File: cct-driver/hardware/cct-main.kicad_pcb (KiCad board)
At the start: 2 copper layers, 110 x 145 mm, 205 parts, among them J1 C707824, J10 C37815, J11 C474923, J2 C165948, J3 C441333, J4 C441333, J5 C441333, J6 C441333, J7 C441333, J8 C441333, J9 C2906270, Q1 C3281500, Q10 C2890395, Q11 C2890395, Q12 C2890395, Q13 C2890395, Q14 C2890395, Q15 C2890395, Q16 C2890395, Q17 C2890395, Q18 C2890395, Q2 C3281500, Q3 C20526, Q4 C2146, Q5 C2146, Q6 C20526, Q7 C2890395, Q8 C2890395, Q9 C2890395, SW1 C318884, SW2 C318884, U1 C2864837, U2 C524806, U3 C6186, U4 C701341, U5 C84681, U6 C52140501, U7 C52140501

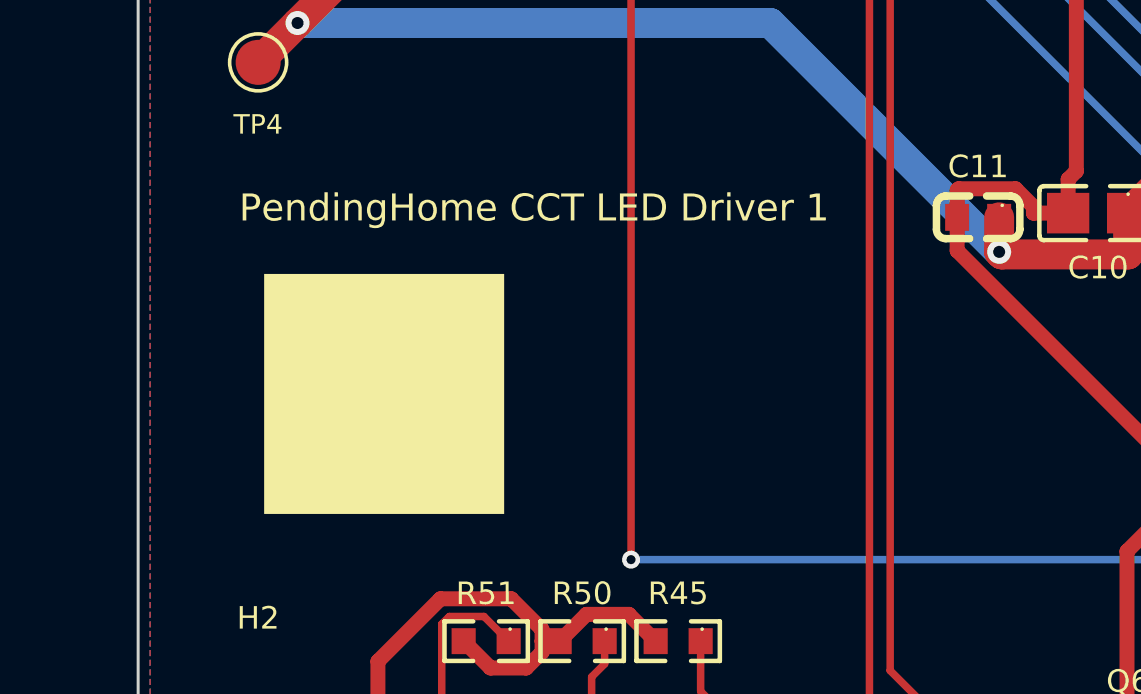
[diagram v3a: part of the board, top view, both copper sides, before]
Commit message: 板名改成白油块右侧两行
按人类要求把 `PendingHome CCT LED Driver 1` 拆成两行放到订单二维码白油块的
右侧:上行 `PendingHome`、下行 `CCT LED Driver 1`,左端对齐,与白块垂直居中。
原来那一行是单行横排压在白块上方,横跨 x2.26–24.14。

实现在 gen_silk.py 里(不手改 kicad_pcb):
- label() 加 left=True,用 KiCad 自己的左对齐,不靠脚本那套估算宽度去凑,
  两行左端因此严格对齐在 x=13.2
- 板名单独抽成 board_name(),常数写在一处:NAME_X=13.2(离白块右沿 1.0mm)、
  NAME_CY=53.2(= 白块中心)、size 0.9 bold、行距 1.5mm(字高 0.9,行间净空 0.6)
- 新增 `--boardname-only` 模式,**幂等**:先删掉板上已有的板名文字再放新的,
  重跑结果一模一样,不会像整份 gen_silk 那样重复堆文字
- 顺带补上一处漏洞:原来的障碍收集只看封装自带丝印,**板级丝印图形(那块白油)
  根本没进障碍表**。现在加进去了,所以「离白块 1.0mm」是真量出来的
- 放之前逐行实测净空并 assert,两行报出来的最近障碍都是白油块、都是 1.00mm

验收数字:
- 除 F_Silkscreen 外**全部 10 层逐字节相同**(F_Cu / B_Cu / F_Mask / B_Mask /
  F_Paste / B_Paste / B_Silkscreen / Edge_Cuts / PTH.drl / NPTH.drl,剔头部时间戳)
- F_Silkscreen 坐标点数 19382 → 19382 不变;差异点 424 出 424 进,
  出的包围盒 (2.66,46.51)–(23.79,47.71) = 旧那一行,
  进的包围盒 (13.49,51.96)–(24.89,54.36) = 新那两行,**全板其余丝印一个点没动**
- cpl-jlc.csv / pos-raw.csv / bom-jlc.csv / bom.csv **零变化**
- DRC 88 → 88 条,七类逐项相同,丝印三类 53/10/9 一条没多;netclass 检查通过
- 渲染出图看过:两行在白块右侧、左端齐、正读、上下不压 C10/R5/C11 与 R51/R50/R45

order-checklist 的认包特征跟着更新:F_Silkscreen 495,581 → **495,768 字节**,
「怎么认这个包」和下单前必查里的板名描述改成两行+右侧+实测坐标范围。
render-top/bottom.png 重新生成。

Co-Authored-By: Claude <noreply@anthropic.com>
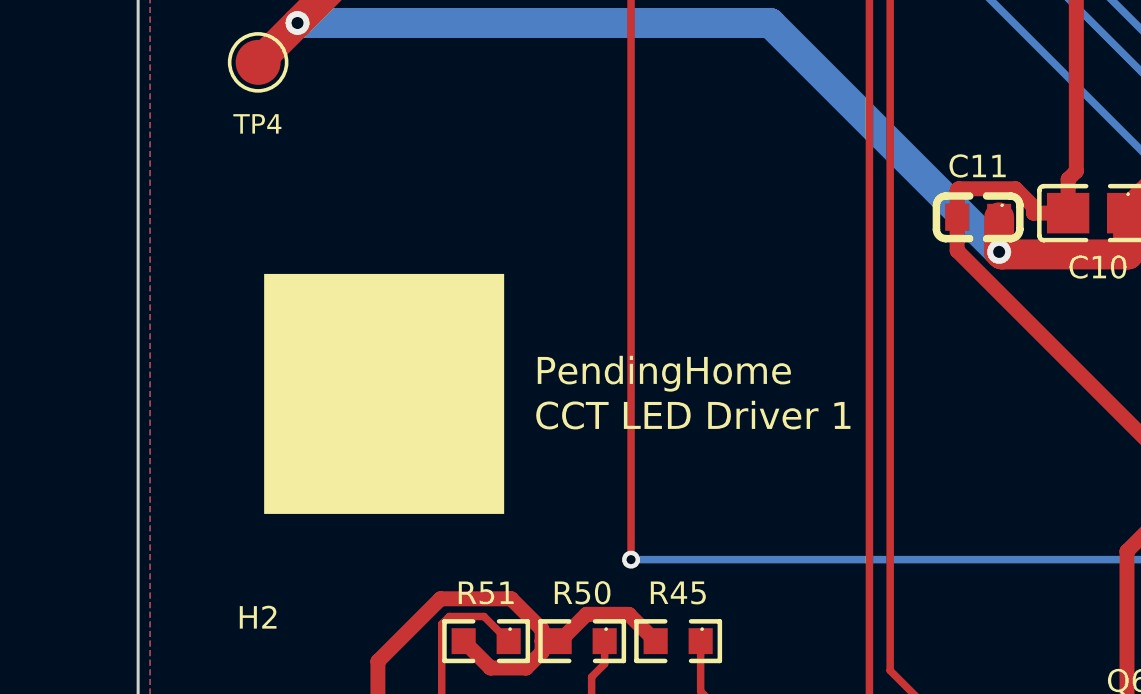
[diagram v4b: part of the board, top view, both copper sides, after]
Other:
- board text added: "CCT LED Driver 1"
- board text added: "PendingHome"
- board text removed: "PendingHome CCT LED Driver 1"
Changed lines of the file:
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@@
 	)
 	(gr_rect
-		(start 12.2 57.2)
-		(end 4.2 49.2)
+		(start 4.2 49.2)
+		(end 12.2 57.2)
 		(stroke
 			(width 0)
@@
 		)
 	)
-	(gr_text "PendingHome CCT LED Driver 1"
-		(at 13.2 47 0)
+	(gr_text "PendingHome"
+		(at 13.2 52.45 0)
 		(layer "F.SilkS")
 		(effects
@@
 				(thickness 0.18)
 			)
-		)
-	)
+			(justify left)
+		)
+	)
+	(gr_text "CCT LED Driver 1"
+		(at 13.2 53.95 0)
+		(layer "F.SilkS")
+		(effects
+			(font
+				(size 0.9 0.9)
+				(thickness 0.18)
+			)
+			(justify left)
+		)
+	)
